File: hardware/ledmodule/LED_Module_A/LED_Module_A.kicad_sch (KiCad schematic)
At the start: 147 parts, among them U1 DS18B20U+

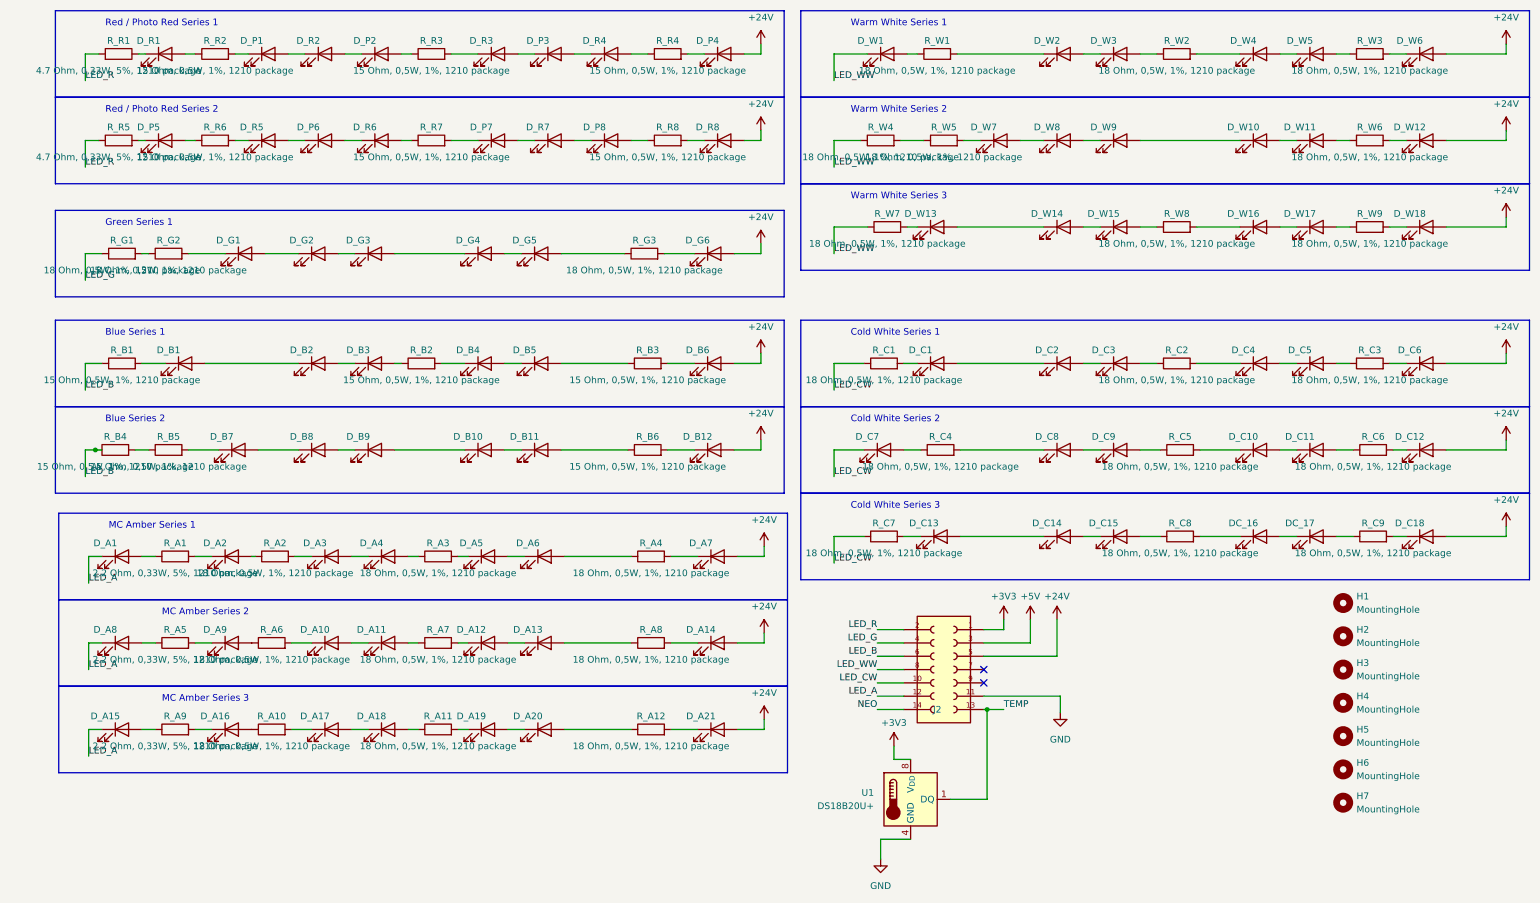
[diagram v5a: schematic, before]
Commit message: Exchange out-of-stock LEDs by alternatives, clean up parts table.
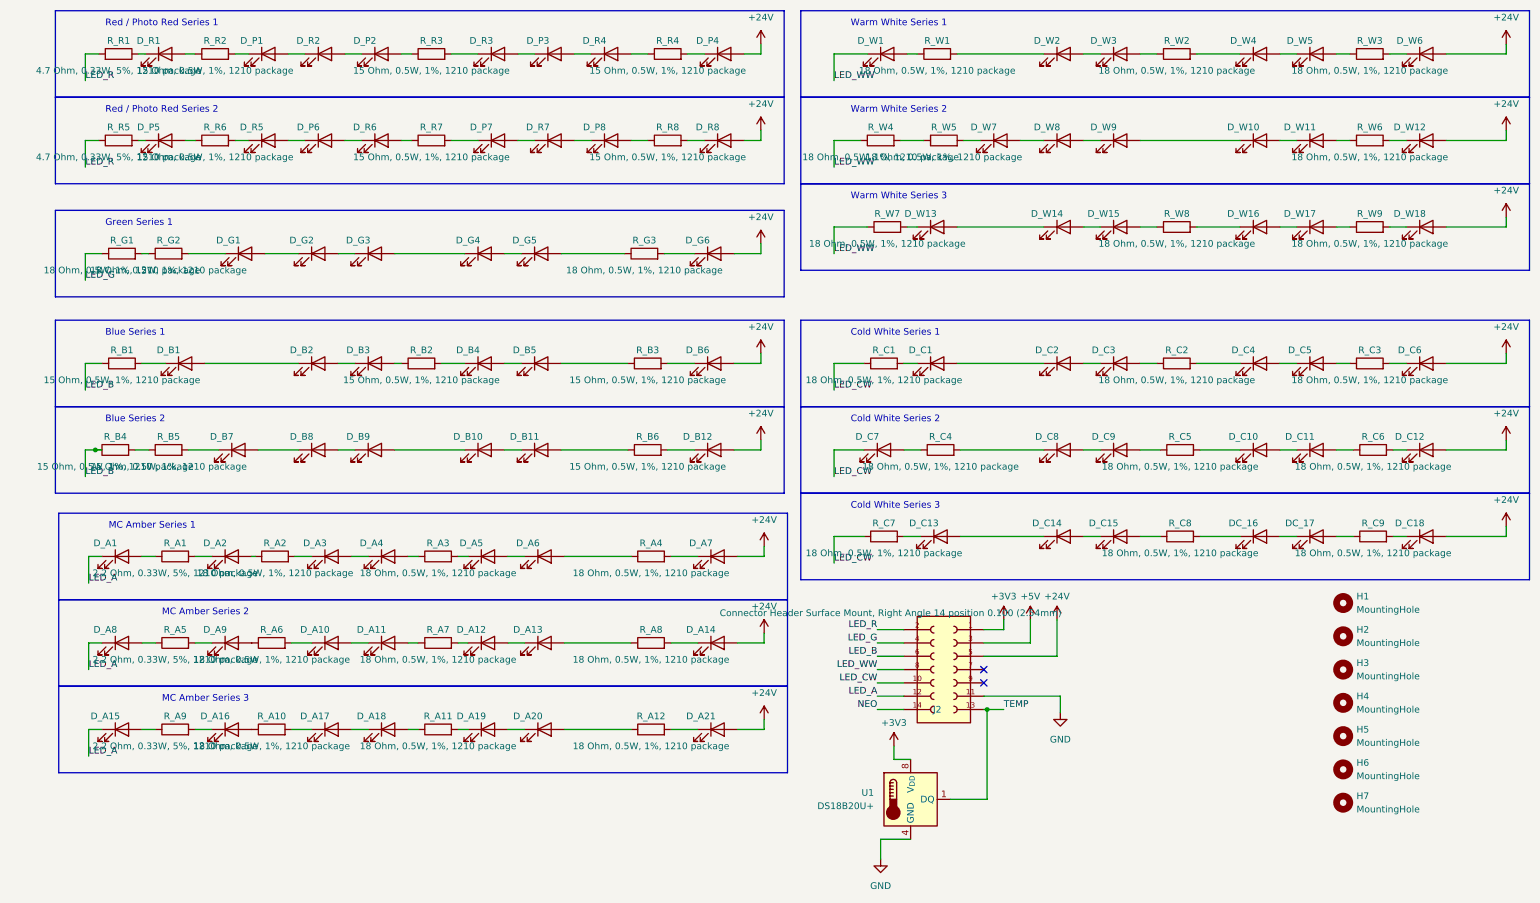
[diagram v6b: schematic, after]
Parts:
- DC_16, DC_17, D_C1, D_C10, D_C11, D_C12, D_C13, D_C14, D_C15, D_C18, D_C2, D_C3, D_C4, D_C5, D_C6, D_C7, D_C8, D_C9: Mouser Part 941-JE2835BWTNU57GAN -> 941-JE2835BWTNU57EAN; Note (none) -> Big Cathode; Part Number JE2835BWT-N-U57GA0000-N0000001 -> JE2835BWT-N-U57EA0000-N0000001
- D_A1, D_A10, D_A11, D_A12, D_A13, D_A14, D_A15, D_A16, D_A17, D_A18, D_A19, D_A2, D_A20, D_A21, D_A3, D_A4, D_A5, D_A6, D_A7, D_A8, D_A9, D_P1, D_P2, D_P3, D_P4, D_P5, D_P6, D_P7, D_P8, D_R1, D_R2, D_R3, D_R4, D_R5, D_R6, D_R7, D_R8: Note (none) -> Big Anode
- D_B1, D_B10, D_B11, D_B12, D_B2, D_B3, D_B4, D_B5, D_B6, D_B7, D_B8, D_B9: value Blue -> Royal Blue; Mouser Part 941-JE2835ABLN05AN -> 941-JE2835ARYN02AN; Note (none) -> Big Cathode; Part Number JE2835ABL-N-0005A0000-N0000001 -> JE2835ARY-N-0002A0000-N0000001
- D_G1, D_G2, D_G3, D_G4, D_G5, D_G6, D_W1, D_W10, D_W11, D_W12, D_W13, D_W14, D_W15, D_W16, D_W17, D_W18, D_W2, D_W3, D_W4, D_W5, D_W6, D_W7, D_W8, D_W9: Note (none) -> Big Cathode
- H1, H2, H3, H4, H5, H6, H7: Note Just drill, no part to place -> DNP; Specification MountingHole -> (none)
- J2: value ~ -> Connector Header Surface Mount, Right Angle 14 position 0.100 (2.54mm); Availability In Stock -> (none); Check_prices https://www.snapeda.com/parts/610114249121/Wurth+Elektronik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 -> (none); MF Wurth Elektronik -> (none); MP 610114249121 -> (none); Manufacturer (none) -> Wuerth Electronic; Package None -> (none); Price None -> (none); Purchase-URL https://www.snapeda.com/api/url_track_click_mouser/?unipart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 -> (none); SnapEDA_Link https://www.snapeda.com/parts/610114249121/Wurth+Elektronik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 -> (none)
- R_A1, R_A5, R_A9: value 2.2 Ohm, 0,33W, 5%, 1210 package -> 2.2 Ohm, 0.33W, 5%, 1210 package; Specification 2.2 Ohm, 0,33W, 5%, 1210 package -> (none)
- R_A10, R_A11, R_A12, R_A2, R_A3, R_A4, R_A6, R_A7, R_A8, R_C1, R_C2, R_C3, R_C4, R_C5, R_C6, R_C7, R_C8, R_C9, R_G1, R_G2, R_G3, R_W1, R_W2, R_W3, R_W4, R_W5, R_W6, R_W7, R_W8, R_W9: value 18 Ohm, 0,5W, 1%, 1210 package -> 18 Ohm, 0.5W, 1%, 1210 package; Specification 18 Ohm, 0,5W, 1%, 1210 package -> (none)
- R_B1, R_B2, R_B3, R_B4, R_B5, R_B6, R_R2, R_R3, R_R4, R_R6, R_R7, R_R8: value 15 Ohm, 0,5W, 1%, 1210 package -> 15 Ohm, 0.5W, 1%, 1210 package; Specification 15 Ohm, 0,5W, 1%, 1210 package -> (none)
- R_R1, R_R5: value 4.7 Ohm, 0,33W, 5%, 1210 package -> 4.7 Ohm, 0.33W, 5%, 1210 package; Specification 4.7 Ohm, 0,33W, 5%, 1210 package -> (none)
- U1: Note Only original parts -> DNP

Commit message: Last changes before ordering again.
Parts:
- H1, H2, H3, H4, H5, H6, H7: Part Number (none) -> DNP; now left out of the parts list
- J2: Part Number (none) -> 710-610114249121
- U1: Part Number DS18B20U+ -> DNP; now not fitted
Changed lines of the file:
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@@
   )
   (symbol (lib_id "Mechanical:MountingHole") (at 260.985 148.59 0) (unit 1)
-    (in_bom yes) (on_board yes) (dnp no) (fields_autoplaced)
+    (in_bom no) (on_board yes) (dnp no) (fields_autoplaced)
     (property "Reference" "H4" (at 263.525 147.32 0)
       (effects (font (size 1.27 1.27)) (justify left))
@@
       (effects (font (size 1.27 1.27)) hide)
     )
-    (property "Part Number" "" (at 260.985 148.59 0)
+    (property "Part Number" "DNP" (at 260.985 148.59 0)
       (effects (font (size 1.27 1.27)) hide)
     )
@@
   )
   (symbol (lib_id "Mechanical:MountingHole") (at 260.985 154.94 0) (unit 1)
-    (in_bom yes) (on_board yes) (dnp no) (fields_autoplaced)
+    (in_bom no) (on_board yes) (dnp no) (fields_autoplaced)
     (property "Reference" "H5" (at 263.525 153.67 0)
       (effects (font (size 1.27 1.27)) (justify left))
@@
       (effects (font (size 1.27 1.27)) hide)
     )
-    (property "Part Number" "" (at 260.985 154.94 0)
+    (property "Part Number" "DNP" (at 260.985 154.94 0)
       (effects (font (size 1.27 1.27)) hide)
     )
@@
   )
   (symbol (lib_id "Mechanical:MountingHole") (at 260.985 161.29 0) (unit 1)
-    (in_bom yes) (on_board yes) (dnp no) (fields_autoplaced)
+    (in_bom no) (on_board yes) (dnp no) (fields_autoplaced)
     (property "Reference" "H6" (at 263.525 160.02 0)
       (effects (font (size 1.27 1.27)) (justify left))
@@
       (effects (font (size 1.27 1.27)) hide)
     )
-    (property "Part Number" "" (at 260.985 161.29 0)
+    (property "Part Number" "DNP" (at 260.985 161.29 0)
       (effects (font (size 1.27 1.27)) hide)
     )
@@
   )
   (symbol (lib_id "Sensor_Temperature:DS18B20U") (at 178.435 167.005 0) (unit 1)
-    (in_bom yes) (on_board yes) (dnp no) (fields_autoplaced)
+    (in_bom yes) (on_board yes) (dnp yes) (fields_autoplaced)
     (property "Reference" "U1" (at 171.45 165.735 0)
       (effects (font (size 1.27 1.27)) (justify right))
@@
       (effects (font (size 1.27 1.27)) hide)
     )
-    (property "Part Number" "DS18B20U+" (at 178.435 167.005 0)
+    (property "Part Number" "DNP" (at 178.435 167.005 0)
       (effects (font (size 1.27 1.27)) hide)
     )
@@
       (effects (font (size 1.27 1.27)) hide)
     )
-    (property "Part Number" "" (at 184.785 142.24 0)
+    (property "Part Number" "710-610114249121 " (at 184.785 142.24 0)
       (effects (font (size 1.27 1.27)) hide)
     )
@@
   )
   (symbol (lib_id "Mechanical:MountingHole") (at 260.985 129.54 0) (unit 1)
-    (in_bom yes) (on_board yes) (dnp no) (fields_autoplaced)
+    (in_bom no) (on_board yes) (dnp no) (fields_autoplaced)
     (property "Reference" "H1" (at 263.525 128.27 0)
       (effects (font (size 1.27 1.27)) (justify left))
@@
       (effects (font (size 1.27 1.27)) hide)
     )
-    (property "Part Number" "" (at 260.985 129.54 0)
+    (property "Part Number" "DNP" (at 260.985 129.54 0)
       (effects (font (size 1.27 1.27)) hide)
     )
@@
   )
   (symbol (lib_id "Mechanical:MountingHole") (at 260.985 135.89 0) (unit 1)
-    (in_bom yes) (on_board yes) (dnp no) (fields_autoplaced)
+    (in_bom no) (on_board yes) (dnp no) (fields_autoplaced)
     (property "Reference" "H2" (at 263.525 134.62 0)
       (effects (font (size 1.27 1.27)) (justify left))
@@
       (effects (font (size 1.27 1.27)) hide)
     )
-    (property "Part Number" "" (at 260.985 135.89 0)
+    (property "Part Number" "DNP" (at 260.985 135.89 0)
       (effects (font (size 1.27 1.27)) hide)
     )
@@
   )
   (symbol (lib_id "Mechanical:MountingHole") (at 260.985 142.24 0) (unit 1)
-    (in_bom yes) (on_board yes) (dnp no) (fields_autoplaced)
+    (in_bom no) (on_board yes) (dnp no) (fields_autoplaced)
     (property "Reference" "H3" (at 263.525 140.97 0)
       (effects (font (size 1.27 1.27)) (justify left))
@@
       (effects (font (size 1.27 1.27)) hide)
     )
-    (property "Part Number" "" (at 260.985 142.24 0)
+    (property "Part Number" "DNP" (at 260.985 142.24 0)
       (effects (font (size 1.27 1.27)) hide)
     )
@@
   )
   (symbol (lib_id "Mechanical:MountingHole") (at 260.985 167.64 0) (unit 1)
-    (in_bom yes) (on_board yes) (dnp no) (fields_autoplaced)
+    (in_bom no) (on_board yes) (dnp no) (fields_autoplaced)
     (property "Reference" "H7" (at 263.525 166.37 0)
       (effects (font (size 1.27 1.27)) (justify left))
@@
       (effects (font (size 1.27 1.27)) hide)
     )
-    (property "Part Number" "" (at 260.985 167.64 0)
+    (property "Part Number" "DNP" (at 260.985 167.64 0)
       (effects (font (size 1.27 1.27)) hide)
     )
